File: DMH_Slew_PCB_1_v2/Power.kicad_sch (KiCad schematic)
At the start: 29 parts, among them J0 Conn_01x01, J101 IDC_02x08, J200 IDC_02x05, J50 Conn_01x08_PinHeader, J51 Conn_01x08_PinHeader, J60 Conn_01x08_PinHeader, J61 Conn_01x08_PinHeader, U1 TL074, U10 LM4040LP-10, U11 LM4040LP-10, U2 TL074, U3 TL074, U4 TL074

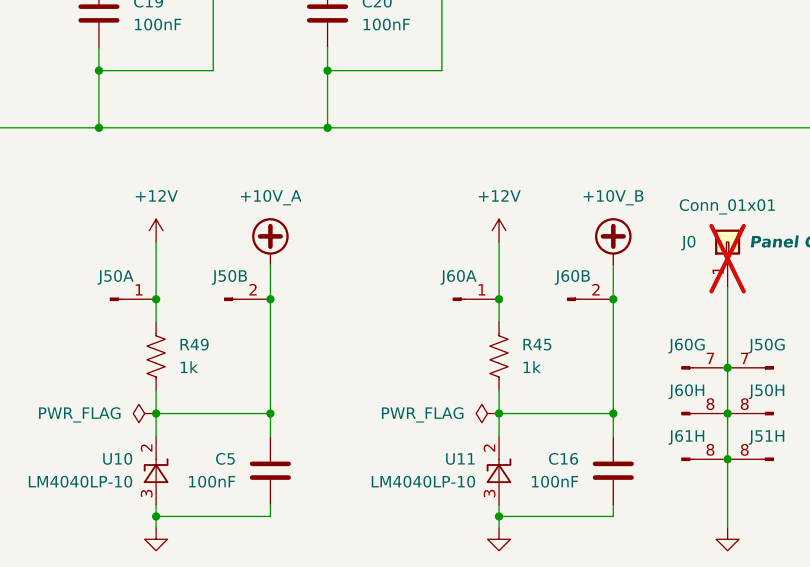
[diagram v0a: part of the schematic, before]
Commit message: PCB 2 component placement done
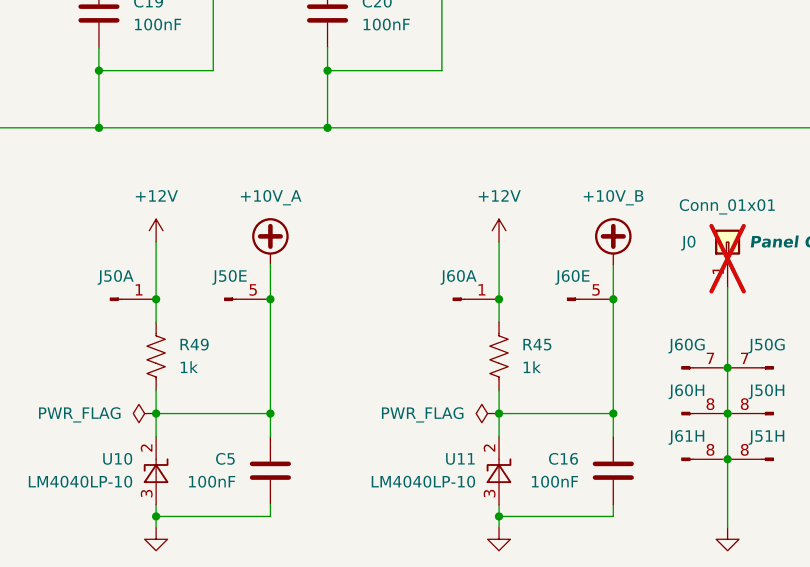
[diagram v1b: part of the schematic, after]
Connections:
- net +10V_A: now also J50.5 (Pin_5); no longer J50.2 (Pin_2)
- net +10V_B: now also J60.5 (Pin_5); no longer J60.2 (Pin_2)
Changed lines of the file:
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@@
 		(lib_id "SynthStuff:Conn_01x08_PinHeader")
 		(at 140.97 165.1 0)
-		(unit 2)
+		(unit 5)
 		(exclude_from_sim no)
 		(in_bom yes)
@@
 				(path "/58f4306d-5387-4983-bb08-41a2313fd315/0cdf34b2-39cd-4d9e-981a-97cd34791509"
 					(reference "J60")
-					(unit 2)
+					(unit 5)
 				)
 			)
@@
 		(lib_id "SynthStuff:Conn_01x08_PinHeader")
 		(at 102.87 165.1 0)
-		(unit 2)
+		(unit 5)
 		(exclude_from_sim no)
 		(in_bom yes)
@@
 				(path "/58f4306d-5387-4983-bb08-41a2313fd315/0cdf34b2-39cd-4d9e-981a-97cd34791509"
 					(reference "J50")
-					(unit 2)
-				)
-			)
+					(unit 5)
+				)
+			)

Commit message: PCB 1 component placement ongoing
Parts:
- J0: Function Panel GND -> GND
- U1, U3: footprint Package_DIP:DIP-16_W7.62mm_Socket -> Package_DIP:DIP-14_W7.62mm_Socket
- renumbered J101 to J100
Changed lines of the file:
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@@
 			)
 		)
-		(property "Function" "Panel GND"
-			(at 166.37 158.75 90)
+		(property "Function" "GND"
+			(at 163.322 158.75 90)
 			(effects
 				(font
@@
 			)
 		)
-		(property "Footprint" "Package_DIP:DIP-16_W7.62mm_Socket"
+		(property "Footprint" "Package_DIP:DIP-14_W7.62mm_Socket"
 			(at 102.87 118.11 0)
 			(effects
@@
 			)
 		)
-		(property "Footprint" "Package_DIP:DIP-16_W7.62mm_Socket"
+		(property "Footprint" "Package_DIP:DIP-14_W7.62mm_Socket"
 			(at 52.07 118.11 0)
 			(effects
@@
 		(dnp no)
 		(fields_autoplaced yes)
-		(property "Reference" "J101"
+		(property "Reference" "J100"
 			(at 25.4 168.91 0)
 			(effects
@@
 			(project "DMH-Kosmo-10cm-PCB"
 				(path "/58f4306d-5387-4983-bb08-41a2313fd315/0cdf34b2-39cd-4d9e-981a-97cd34791509"
-					(reference "J101")
+					(reference "J100")
 					(unit 1)
 				)

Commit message: Updated Log circuit
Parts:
- renumbered J60 to J50, J61 to J51, J50 to J60, J51 to J61
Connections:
- net +12V: no longer J50.1 (Pin_1), J60.1 (Pin_1)
- net GND: now also J50.1 (Pin_1), J60.1 (Pin_1)
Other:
- moved on the sheet: J50G, J50H, J51H, J60G, J60H, J61H
